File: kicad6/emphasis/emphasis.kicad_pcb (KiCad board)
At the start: 2 copper layers, 114.1 x 129 mm, 40 parts, among them J1 EMPH_IN, J10 Conn_01x03_Female, J11 Conn_01x03_Male, J12 Conn_01x03_Male, J13 Conn_01x20_Male, J14 Conn_02x05, J2 DIST_IN, J3 DE_EMPH_IN, J4 EMPH_OUT, J5 DIST_OUT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

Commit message: emphasis pin shuffling
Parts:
- added R8: 22k, Resistor_THT:R_Axial_DIN0207_L6.3mm_D2.5mm_P10.16mm_Horizontal, F.Cu at (149.9, 99.1)
- D1, D2, D3, D4: value LED 1.9V -> 1N4148; footprint LED_THT:LED_D3.0mm_FlatTop -> Diode_THT:D_DO-35_SOD27_P7.62mm_Horizontal
- R2: value 100k -> 47k
- R3: value 47k -> 10k
- R4: value 1k -> 2.2k
- R6: value 10k -> 47k
- moved D2 21.7 mm to (149.9, 73.7), turned to -90 degrees
- moved D1 16.1 mm to (154.9, 81.3), turned to 90 degrees
- moved R3 15.2 mm to (142.2, 88.9)
- moved D3 5.68 mm to (180.3, 45.7)
- moved J9 4.84 mm to (58.4, 125.0)
- moved R5 3.59 mm to (175.3, 50.8)
- moved R7 3.59 mm to (149.9, 111.8)
- moved D4 3.59 mm to (177.8, 53.3)
- moved R6 3.59 mm to (165.1, 53.3)
- moved C1 2.54 mm to (180.3, 91.4)
- moved C2 2.54 mm to (170.2, 91.4)
- moved C4 2.54 mm to (162.6, 66.0)
- moved JP2 2.54 mm to (124.5, 114.3)
- moved RV3 2.54 mm to (86.3, 63.5)
- moved U1 2.54 mm to (142.5, 77.8)
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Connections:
- J13 pad 10: GND -> unconnected-(J13-Pad10)
- J13 pad 17: unconnected-(J13-Pad17) -> /SHELF_2
- J13 pad 18: /SHELF_2 -> /SHELF_1
- J13 pad 19: /SHELF_1 -> unconnected-(J13-Pad19)
- J13 pad 2: unconnected-(J13-Pad2) -> /FREQ_POT
- J13 pad 3: /FREQ_POT -> /EMPH_POT
- J13 pad 4: /EMPH_POT -> unconnected-(J13-Pad4)
- J13 pad 5: unconnected-(J13-Pad5) -> +5V
- J13 pad 6: +5V -> unconnected-(J13-Pad6)
- J13 pad 7: unconnected-(J13-Pad7) -> GND
- J8 pad 10: GND -> unconnected-(J8-Pad10)
- J8 pad 17: unconnected-(J8-Pad17) -> Net-(J8-Pad17)
- J8 pad 18: Net-(SW1-Pad1) -> Net-(J8-Pad18)
- J8 pad 19: Net-(SW1-Pad3) -> unconnected-(J8-Pad19)
- J8 pad 2: unconnected-(J8-Pad2) -> /FREQ_POT
- J8 pad 3: /FREQ_POT -> /EMPH_POT
- J8 pad 4: /EMPH_POT -> unconnected-(J8-Pad4)
- J8 pad 5: unconnected-(J8-Pad5) -> +5V
- J8 pad 6: +5V -> unconnected-(J8-Pad6)
- J8 pad 7: unconnected-(J8-Pad7) -> GND
- SW1 pad 1: Net-(SW1-Pad1) -> Net-(J8-Pad17)
- SW1 pad 3: Net-(SW1-Pad3) -> Net-(J8-Pad18)
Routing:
- net GND: track 389.9 -> 422.9 mm, vias 6 -> 8
- net Net-(J8-Pad17): track 0.00 -> 22.9 mm
- net /LED_clipper/SC_jumper_out: track 17.8 -> 38.1 mm
- net Net-(SW1-Pad1): track 20.3 -> 0.00 mm
- net Net-(J8-Pad18): track 0.00 -> 15.2 mm
- net Net-(SW1-Pad3): track 12.7 -> 0.00 mm
- net Net-(D1-Pad2): track 17.8 -> 27.9 mm, vias 0 -> 2
- net Net-(C5-Pad1): track 94.0 -> 88.9 mm, vias 4 -> 3
- net /FREQ_POT: track 79.3 -> 76.7 mm
- net /CV_POT: track 53.9 -> 51.3 mm
- net /CV_DEST: track 40.8 -> 43.3 mm
- net Net-(C6-Pad1): track 17.8 -> 20.4 mm
- net /CV_JACK: track 41.6 -> 39.5 mm
- net +5V: vias 6 -> 5
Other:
- outline, holes or cut-outs redrawn

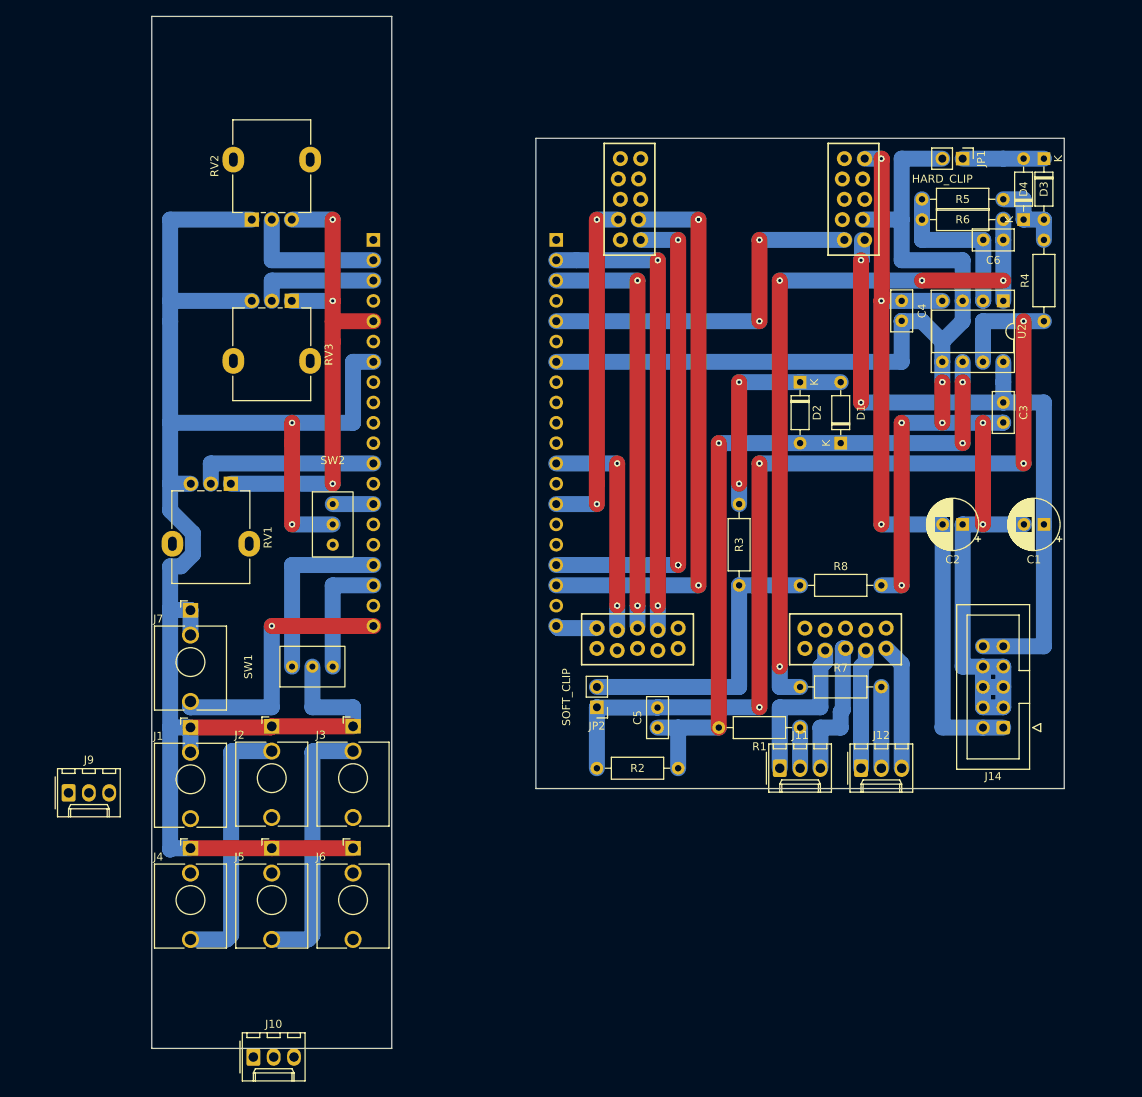
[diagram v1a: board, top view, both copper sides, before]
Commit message: Emphasis: flipped board, take 1
Not entirely happy with the way this is going, might start again.

Basically I messed up the orientation of the main board relative to
the control board: to avoid having the patch_sm stick out the side,
parts need to be mounted on the "back" of main board. But this flips
the orientation of patch_sm and ICs, so everything needs to be
re-routed.
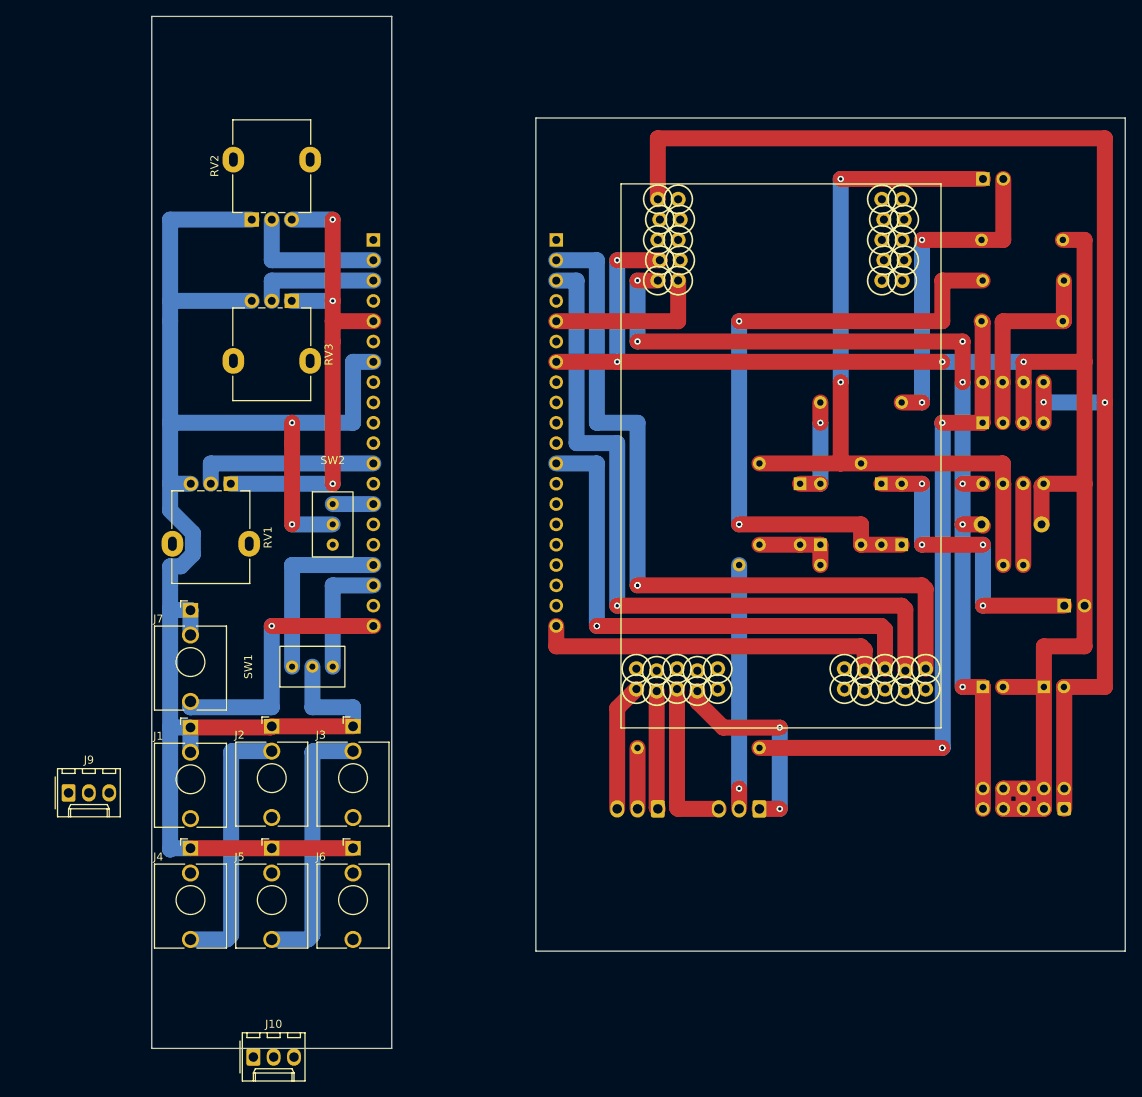
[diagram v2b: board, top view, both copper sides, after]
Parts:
- C1, C2, C4, C5, C6, D1, D2, D3, D4, J11, J12, J14, JP1, JP2, R1, R2, R3, R4, R5, R6, R8, U2: moved to B.Cu
- C3: footprint Capacitor_THT:C_Disc_D5.0mm_W2.5mm_P2.50mm -> Capacitor_THT:C_Disc_D7.5mm_W5.0mm_P7.50mm; moved to B.Cu
- R7: footprint Resistor_THT:R_Axial_DIN0207_L6.3mm_D2.5mm_P10.16mm_Horizontal -> Resistor_THT:R_Axial_DIN0207_L6.3mm_D2.5mm_P15.24mm_Horizontal; moved to B.Cu
- U1: moved to F.Cu
- moved JP2 81.8 mm to (172.7, 48.3), turned to -90 degrees
- moved JP1 57.3 mm to (182.9, 101.6)
- moved C5 50.0 mm to (177.8, 96.5), turned to 180 degrees
- moved R8 48.8 mm to (172.5, 55.9)
- moved D3 45.4 mm to (160.0, 86.4)
- moved D4 43.4 mm to (162.6, 94.0)
- moved R2 29.7 mm to (144.8, 94.0), turned to 90 degrees
- moved R4 29.0 mm to (157.5, 83.8), turned to -90 degrees
- moved J12 25.9 mm to (132.1, 127.0), turned to 180 degrees
- moved C2 22.7 mm to (180.3, 111.8), turned to 0 degrees
- moved R6 21.7 mm to (182.7, 66.0), turned to 180 degrees
- moved C1 21.7 mm to (172.7, 111.8), turned to 0 degrees
- moved R1 21.7 mm to (142.2, 96.5), turned to 0 degrees
- moved C6 17.9 mm to (175.2, 73.7), turned to 180 degrees
- moved C4 17.1 mm to (177.8, 73.7), turned to 0 degrees
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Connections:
- U1 pad C6: /CV_JACK -> /FREQ_POT
- U1 pad C7: /CV_POT -> /EMPH_POT
- U1 pad C8: /EMPH_POT -> /CV_POT
- U1 pad C9: /FREQ_POT -> /CV_JACK
- U1 pad D3: unconnected-(U1-PadD3) -> /CV_DEST
- U1 pad D4: /SHELF_1 -> /SHELF_2
- U1 pad D5: /SHELF_2 -> /SHELF_1
- U1 pad D7: /CV_DEST -> unconnected-(U1-PadD7)
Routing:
- net Net-(D3-Pad2): track 10.2 -> 83.8 mm, vias 0 -> 3
- net /SHELF_1: track 71.0 -> 0.00 mm, vias 3 -> 0
- net -12V: track 96.1 -> 165.2 mm, vias 3 -> 2
- net Net-(C5-Pad1): track 88.9 -> 20.3 mm, vias 3 -> 0
- net /SHELF_2: track 60.6 -> 0.00 mm, vias 3 -> 0
- net /CV_DEST: track 43.3 -> 0.00 mm, vias 2 -> 0
- net /EMPH_POT: track 68.6 -> 107.4 mm, vias 2 -> 1
- net /CV_JACK: track 39.5 -> 78.2 mm
- net /CV_POT: track 51.3 -> 89.4 mm
- net /FREQ_POT: track 76.7 -> 114.8 mm
- net +12V: track 86.4 -> 116.9 mm, vias 2 -> 7
- net /LED_clipper/hard_clipping_sink: track 10.2 -> 38.1 mm, vias 0 -> 4
- net +5V: track 107.3 -> 81.4 mm, vias 5 -> 3
- net /LED_clipper/SC_jumper_in: track 122.0 -> 96.5 mm, vias 4 -> 2
- net /LED_clipper/Clipper_in: track 5.08 -> 30.5 mm, vias 0 -> 1
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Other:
- board size 114.1 x 129 mm -> 121.7 x 129 mm
- board text removed: "HARD_CLIP"
- board text removed: "SOFT_CLIP"

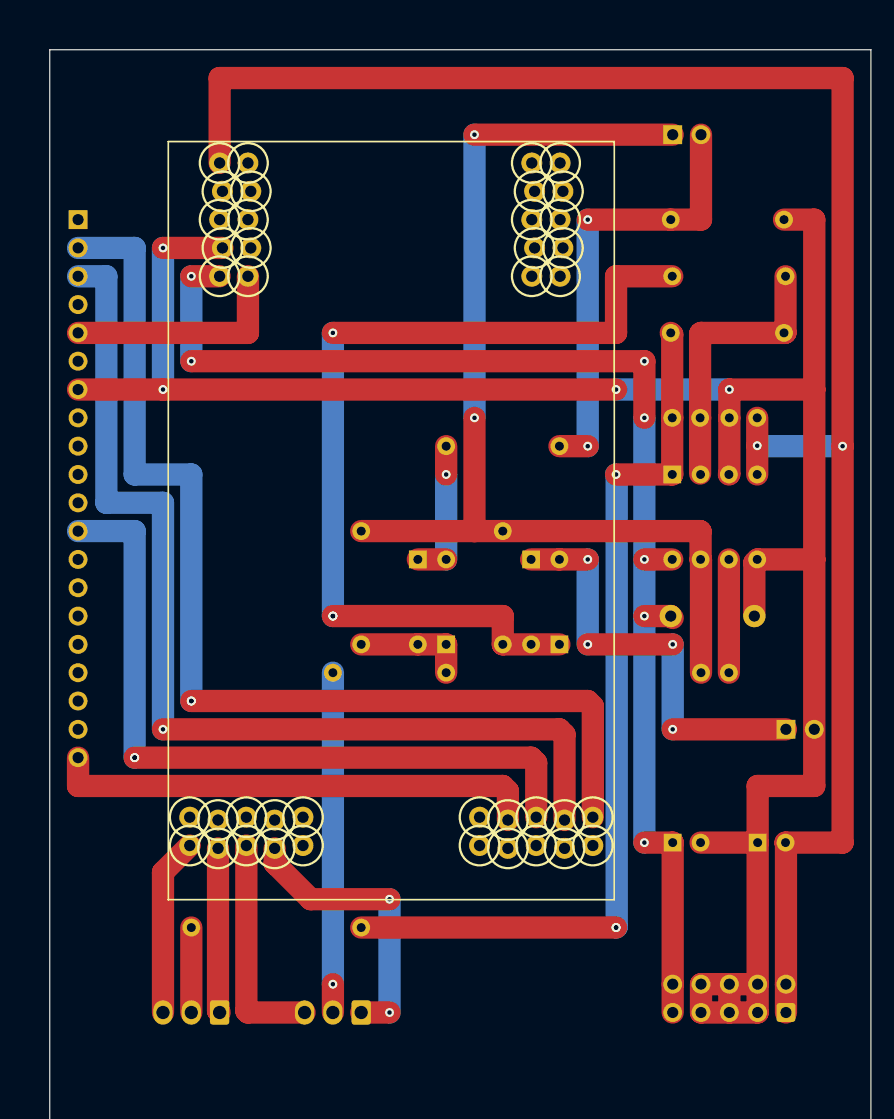
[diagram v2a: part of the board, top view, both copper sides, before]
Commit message: Emphasis take 3: flipped components, cleaner layout
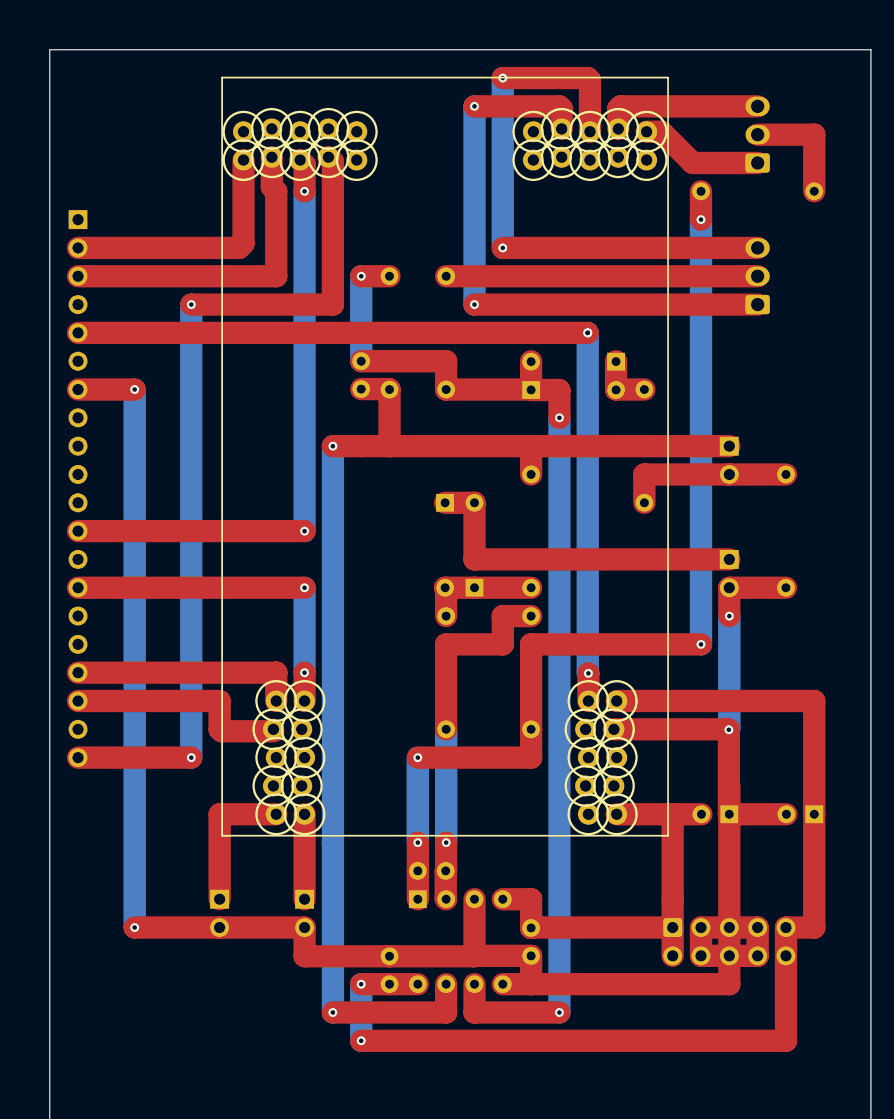
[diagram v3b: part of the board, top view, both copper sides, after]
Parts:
- added JP3: Jumper_2_Bridged, Connector_PinHeader_2.54mm:PinHeader_1x02_P2.54mm_Vertical, B.Cu at (139.7, 116.8)
- added JP4: Jumper_2_Bridged, Connector_PinHeader_2.54mm:PinHeader_1x02_P2.54mm_Vertical, B.Cu at (132.1, 116.8)
- C3: footprint Capacitor_THT:C_Disc_D7.5mm_W5.0mm_P7.50mm -> Capacitor_THT:C_Disc_D5.0mm_W2.5mm_P2.50mm
- R7: footprint Resistor_THT:R_Axial_DIN0207_L6.3mm_D2.5mm_P15.24mm_Horizontal -> Resistor_THT:R_Axial_DIN0207_L6.3mm_D2.5mm_P10.16mm_Horizontal
- moved J12 90.2 mm to (180.3, 50.8), turned to 90 degrees
- moved J11 72.8 mm to (180.3, 63.5), turned to 90 degrees
- moved R7 72.7 mm to (175.3, 53.3), turned to 0 degrees
- moved C4 51.4 mm to (160.0, 121.9), turned to 90 degrees
- moved C6 46.6 mm to (152.4, 114.3)
- moved U2 44.4 mm to (149.9, 116.8)
- moved C5 43.2 mm to (144.8, 68.6), turned to -90 degrees
- moved C3 41.6 mm to (147.3, 124.5), turned to 90 degrees
- moved R1 37.0 mm to (152.4, 61.0), turned to -90 degrees
- moved R5 36.6 mm to (152.4, 91.4), turned to -90 degrees
- moved R6 34.1 mm to (160.0, 91.4), turned to -90 degrees
- moved R2 33.1 mm to (147.3, 61.0), turned to -90 degrees
- moved JP2 28.4 mm to (177.8, 76.2), turned to 180 degrees
- moved D2 25.1 mm to (167.6, 68.6), turned to 180 degrees
- moved R8 25.1 mm to (182.9, 78.7), turned to -90 degrees
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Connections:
- J12 pad 1: /EMPH_OUT -> /DE_EMPH_OUT
- J12 pad 3: /DE_EMPH_OUT -> /EMPH_OUT
- U1 pad D1: unconnected-(U1-PadD1) -> Net-(U1-PadD1)
- U1 pad D10: unconnected-(U1-PadD10) -> Net-(U1-PadD10)
- U1 pad D3: /CV_DEST -> unconnected-(U1-PadD3)
- U1 pad D4: /SHELF_2 -> unconnected-(U1-PadD4)
- U1 pad D5: /SHELF_1 -> /CV_DEST
- U1 pad D6: unconnected-(U1-PadD6) -> /SHELF_2
- U1 pad D7: unconnected-(U1-PadD7) -> /SHELF_1
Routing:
- net -12V: track 165.2 -> 38.1 mm, vias 2 -> 0
- net Net-(C5-Pad1): track 20.3 -> 99.0 mm, vias 0 -> 3
- net /FREQ_POT: track 114.8 -> 40.3 mm, vias 2 -> 0
- net Net-(D3-Pad2): track 83.8 -> 10.3 mm, vias 3 -> 0
- net /EMPH_POT: track 107.4 -> 43.9 mm, vias 1 -> 0
- net +5V: track 81.4 -> 139.8 mm, vias 3 -> 6
- net /CV_JACK: track 78.2 -> 111.2 mm, vias 1 -> 3
- net /DE_EMPH_IN: track 20.1 -> 50.6 mm, vias 0 -> 2
- net /CV_DEST: track 0.00 -> 30.5 mm, vias 0 -> 2
- net /EMPH_IN: track 25.7 -> 52.9 mm
- net /LED_clipper/SC_jumper_out: track 40.6 -> 15.2 mm, vias 2 -> 0
- net /SHELF_2: track 0.00 -> 20.4 mm
- net /SHELF_1: track 0.00 -> 20.1 mm
- net +12V: track 116.9 -> 99.0 mm, vias 7 -> 2
- net /LED_clipper/SC_jumper_in: track 96.5 -> 109.2 mm
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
